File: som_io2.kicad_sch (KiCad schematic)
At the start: 8 parts, among them J1 Hermaphroditic_Molex_203456-0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, Y1 Oscillator_156.25MHz_SG3225EEN

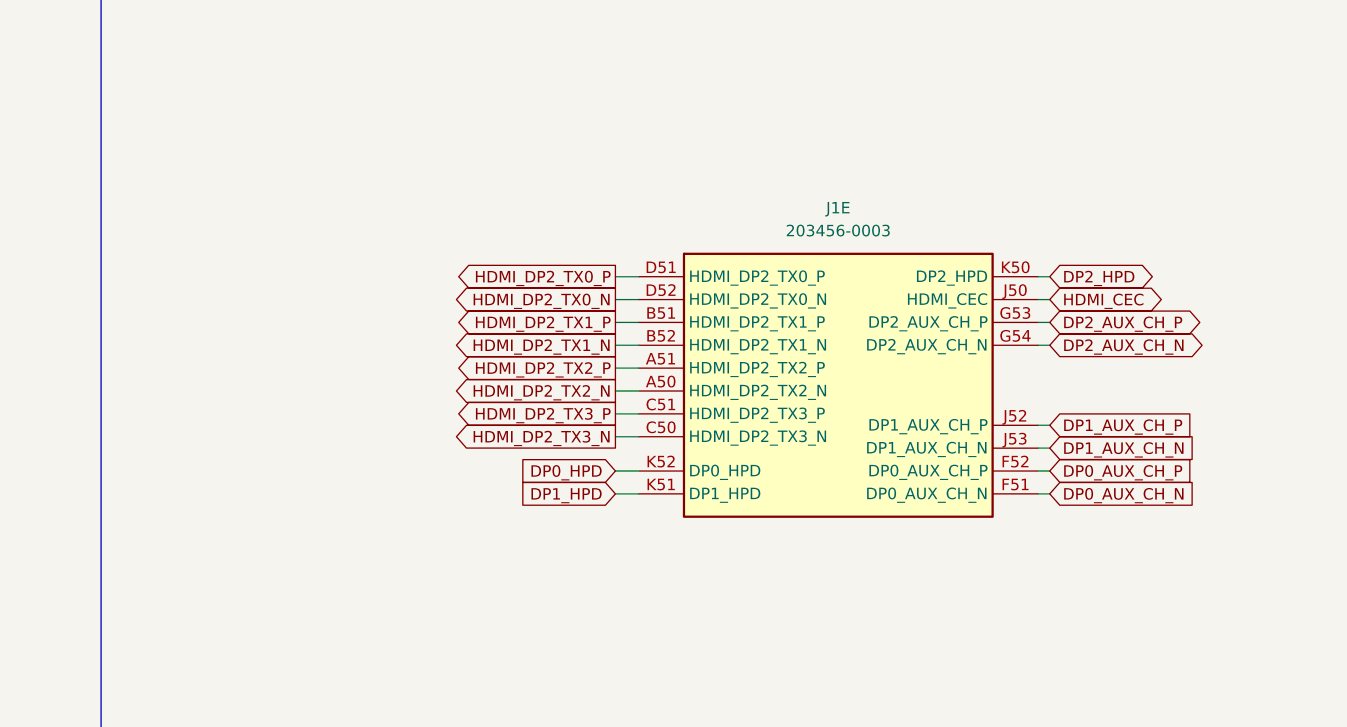
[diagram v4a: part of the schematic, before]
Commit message: [#82837] Start fixing USB DP Alt mode sheet: clean up, define DP bus, rename USB nets and buses to match rest of the schematic
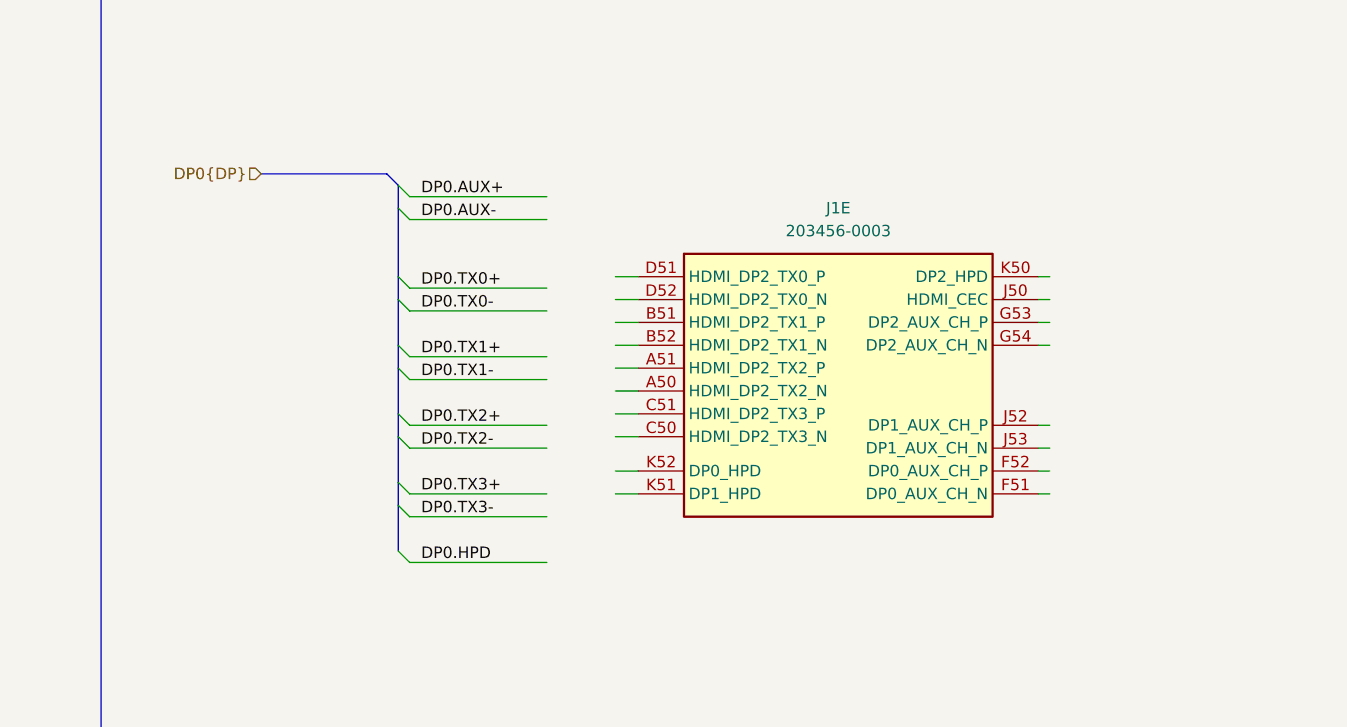
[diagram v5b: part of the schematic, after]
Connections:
- net DP0_AUX_CH_N: no longer names the net of J1.F51 (DP0_AUX_CH_N)
- net DP0_AUX_CH_P: no longer names the net of J1.F52 (DP0_AUX_CH_P)
- net DP0_HPD: no longer names the net of J1.K52 (DP0_HPD)
- net DP1_AUX_CH_N: no longer names the net of J1.J53 (DP1_AUX_CH_N)
- net DP1_AUX_CH_P: no longer names the net of J1.J52 (DP1_AUX_CH_P)
- net DP1_HPD: no longer names the net of J1.K51 (DP1_HPD)
- net DP2_AUX_CH_N: no longer names the net of J1.G54 (DP2_AUX_CH_N)
- net DP2_AUX_CH_P: no longer names the net of J1.G53 (DP2_AUX_CH_P)
- net DP2_HPD: no longer names the net of J1.K50 (DP2_HPD)
- net HDMI_CEC: no longer names the net of J1.J50 (HDMI_CEC)
- net HDMI_DP2_TX0_N: no longer names the net of J1.D52 (HDMI_DP2_TX0_N)
- net HDMI_DP2_TX0_P: no longer names the net of J1.D51 (HDMI_DP2_TX0_P)
- net HDMI_DP2_TX1_N: no longer names the net of J1.B52 (HDMI_DP2_TX1_N)
- net HDMI_DP2_TX1_P: no longer names the net of J1.B51 (HDMI_DP2_TX1_P)
- net HDMI_DP2_TX2_N: no longer names the net of J1.A50 (HDMI_DP2_TX2_N)
- net HDMI_DP2_TX2_P: no longer names the net of J1.A51 (HDMI_DP2_TX2_P)
- net HDMI_DP2_TX3_N: no longer names the net of J1.C50 (HDMI_DP2_TX3_N)
- net HDMI_DP2_TX3_P: no longer names the net of J1.C51 (HDMI_DP2_TX3_P)

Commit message: [#82837] Map interfaces from AGX to Thor on SoM schematic and add level shifters for 1V8 interfaces
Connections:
- net PCIe_{C5x8}.CLK+ is gone; now on net PCIe_{C3x2}.CLK+: J1.F24 (PEX_CLK5_P)
- net PCIe_{C5x8}.CLK- is gone; now on net PCIe_{C3x2}.CLK-: J1.F25 (PEX_CLK5_N)
- net PCIe_{C5x8}.RX0+ is gone; now on net PCIe_{C3x2}.RX0+: J1.D24 (UPHY_RX12_P)
- net PCIe_{C5x8}.RX0- is gone; now on net PCIe_{C3x2}.RX0-: J1.D25 (UPHY_RX12_N)
- net PCIe_{C5x8}.RX1+ is gone; now on net PCIe_{C3x2}.RX1+: J1.B25 (UPHY_RX13_P)
- net PCIe_{C5x8}.RX1- is gone; now on net PCIe_{C3x2}.RX1-: J1.B24 (UPHY_RX13_N)
- net PCIe_{C5x8}.TX0+ is gone; now on net PCIe_{C3x2}.TX0+: J1.H24 (UPHY_TX12_P)
- net PCIe_{C5x8}.TX0- is gone; now on net PCIe_{C3x2}.TX0-: J1.H25 (UPHY_TX12_N)
- net PCIe_{C5x8}.TX1+ is gone; now on net PCIe_{C3x2}.TX1+: J1.K25 (UPHY_TX13_P)
- net PCIe_{C5x8}.TX1- is gone; now on net PCIe_{C3x2}.TX1-: J1.K24 (UPHY_TX13_N)
- net PCIe_{C5x8}.~{CLKREQ} is gone; now on net PCIe_{C3x2}.~{CLKREQ}: J1.C8 (PEX_C5_CLKREQ_N)
- net PCIe_{C5x8}.~{RST} is gone; now on net PCIe_{C3x2}.~{RST}: J1.H10 (PEX_C5_RST_N)
- net PCIe_{C0x1}.CK+ renamed PCIe_{C2x1}.CK+
- net PCIe_{C0x1}.CK- renamed PCIe_{C2x1}.CK-
- net PCIe_{C0x1}.RX0+: no longer names the net of J1.A22 (UPHY_RX0_P)
- net PCIe_{C0x1}.RX0-: no longer names the net of J1.A23 (UPHY_RX0_N)
- net PCIe_{C0x1}.TX0+: no longer names the net of J1.J22 (UPHY_TX0_P)
- net PCIe_{C0x1}.TX0-: no longer names the net of J1.J23 (UPHY_TX0_N)
- net PCIe_{C0x1}.~{CLKREQ} renamed PCIe_{C2x1}.~{CLKREQ}
- net PCIe_{C4x4}.CLK+ renamed PCIe_{C3x2}.CLK+
- net PCIe_{C4x4}.CLK- renamed PCIe_{C3x2}.CLK-
- net PCIe_{C4x4}.RX0+: no longer names the net of J1.D33 (UPHY_RX22_P)
- net PCIe_{C4x4}.RX0-: no longer names the net of J1.D32 (UPHY_RX22_N)
- net PCIe_{C4x4}.RX1+ renamed PCIe_{C2x1}.RX0+
- net PCIe_{C4x4}.RX1- renamed PCIe_{C2x1}.RX0-
- net PCIe_{C4x4}.RX2+ renamed PCIe_{C3x2}.RX0+
- net PCIe_{C4x4}.RX2- renamed PCIe_{C3x2}.RX0-
- net PCIe_{C4x4}.RX3+ renamed PCIe_{C3x2}.RX1+
- net PCIe_{C4x4}.RX3- renamed PCIe_{C3x2}.RX1-
- net PCIe_{C4x4}.TX0+: no longer names the net of J1.J35 (UPHY_TX22_P)
- net PCIe_{C4x4}.TX0-: no longer names the net of J1.J34 (UPHY_TX22_N)
- net PCIe_{C4x4}.TX1+ renamed PCIe_{C2x1}.TX0+
- net PCIe_{C4x4}.TX1- renamed PCIe_{C2x1}.TX0-
- net PCIe_{C4x4}.TX2+ renamed PCIe_{C3x2}.TX0+
- net PCIe_{C4x4}.TX2- renamed PCIe_{C3x2}.TX0-
- net PCIe_{C4x4}.TX3+ renamed PCIe_{C3x2}.TX1+
- net PCIe_{C4x4}.TX3- renamed PCIe_{C3x2}.TX1-
- net PCIe_{C4x4}.~{CLKREQ} renamed PCIe_{C3x2}.~{CLKREQ}
- net PCIe_{C4x4}.~{RST} renamed PCIe_{C3x2}.~{RST}
- net PCIe_{C5x8}.RX2+ renamed PCIe_{C3x2}.RX2+
- net PCIe_{C5x8}.RX2- renamed PCIe_{C3x2}.RX2-
- net PCIe_{C5x8}.RX3+ renamed PCIe_{C3x2}.RX3+
- net PCIe_{C5x8}.RX3- renamed PCIe_{C3x2}.RX3-
- net PCIe_{C5x8}.RX4+: no longer names the net of J1.D28 (UPHY_RX16_P)
- net PCIe_{C5x8}.RX4-: no longer names the net of J1.D29 (UPHY_RX16_N)
- net PCIe_{C5x8}.RX5+: no longer names the net of J1.B29 (UPHY_RX17_P)
- net PCIe_{C5x8}.RX5-: no longer names the net of J1.B28 (UPHY_RX17_N)
- net PCIe_{C5x8}.RX6+: no longer names the net of J1.C31 (UPHY_RX18_P)
- net PCIe_{C5x8}.RX6-: no longer names the net of J1.C30 (UPHY_RX18_N)
- net PCIe_{C5x8}.RX7+: no longer names the net of J1.A30 (UPHY_RX19_P)
- net PCIe_{C5x8}.RX7-: no longer names the net of J1.A31 (UPHY_RX19_N)
- net PCIe_{C5x8}.TX2+ renamed PCIe_{C3x2}.TX2+
- net PCIe_{C5x8}.TX2- renamed PCIe_{C3x2}.TX2-
- net PCIe_{C5x8}.TX3+ renamed PCIe_{C3x2}.TX3+
- net PCIe_{C5x8}.TX3- renamed PCIe_{C3x2}.TX3-
- net PCIe_{C5x8}.TX4+: no longer names the net of J1.H28 (UPHY_TX16_P)
- net PCIe_{C5x8}.TX4-: no longer names the net of J1.H29 (UPHY_TX16_N)
- net PCIe_{C5x8}.TX5+: no longer names the net of J1.K29 (UPHY_TX17_P)
- net PCIe_{C5x8}.TX5-: no longer names the net of J1.K28 (UPHY_TX17_N)
- net PCIe_{C5x8}.TX6+: no longer names the net of J1.G31 (UPHY_TX18_P)
- net PCIe_{C5x8}.TX6-: no longer names the net of J1.G30 (UPHY_TX18_N)
- net PCIe_{C5x8}.TX7+: no longer names the net of J1.J30 (UPHY_TX19_P)
- net PCIe_{C5x8}.TX7-: no longer names the net of J1.J31 (UPHY_TX19_N)
- net RGMII.MDC: no longer names the net of J1.E6 (RGMII_SMA_MDC)
- net RGMII.MDIO: no longer names the net of J1.E7 (RGMII_SMA_MDIO)
- net RGMII.RD0: no longer names the net of J1.C4 (RGMII_RD0)
- net RGMII.RD1: no longer names the net of J1.K6 (RGMII_RD1)
- net RGMII.RD2: no longer names the net of J1.H6 (RGMII_RD2)
- net RGMII.RD3: no longer names the net of J1.E5 (RGMII_RD3)
- net RGMII.RXC: no longer names the net of J1.C5 (RGMII_RXC)
- net RGMII.RX_CTL: no longer names the net of J1.D5 (RGMII_RX_CTL)
- net RGMII.TD0: no longer names the net of J1.J6 (RGMII_TD0)
- net RGMII.TD1: no longer names the net of J1.G5 (RGMII_TD1)
- net RGMII.TD2: no longer names the net of J1.J7 (RGMII_TD2)
- net RGMII.TD3: no longer names the net of J1.G6 (RGMII_TD3)
- net RGMII.TXC: no longer names the net of J1.B5 (RGMII_TXC)
- net RGMII.TX_CTL: no longer names the net of J1.K7 (RGMII_TX_CTL)
- net RGMII.~{INT}: no longer names the net of J1.J5 (ENET_INT)
- net RGMII.~{RST}: no longer names the net of J1.H5 (ENET_RST_N)
- net UPHY_REFCLK0_N: no longer names the net of J1.E31 (UPHY_REFCLK0_N)
- net UPHY_REFCLK0_P: no longer names the net of J1.E30 (UPHY_REFCLK0_P)
- net UPHY_REFCLK1_N: no longer names the net of J1.E26 (UPHY_REFCLK1_N)
- net UPHY_REFCLK1_P: no longer names the net of J1.E27 (UPHY_REFCLK1_P)
- net UPHY_REFCLK3_N: no longer names the net of J1.F33 (UPHY_REFCLK3_N)
- net UPHY_REFCLK3_P: no longer names the net of J1.F32 (UPHY_REFCLK3_P)
- net UPHY_REFCLK4_N: no longer names the net of J1.C38 (UPHY_REFCLK4_N)
- net UPHY_REFCLK4_P: no longer names the net of J1.C39 (UPHY_REFCLK4_P)

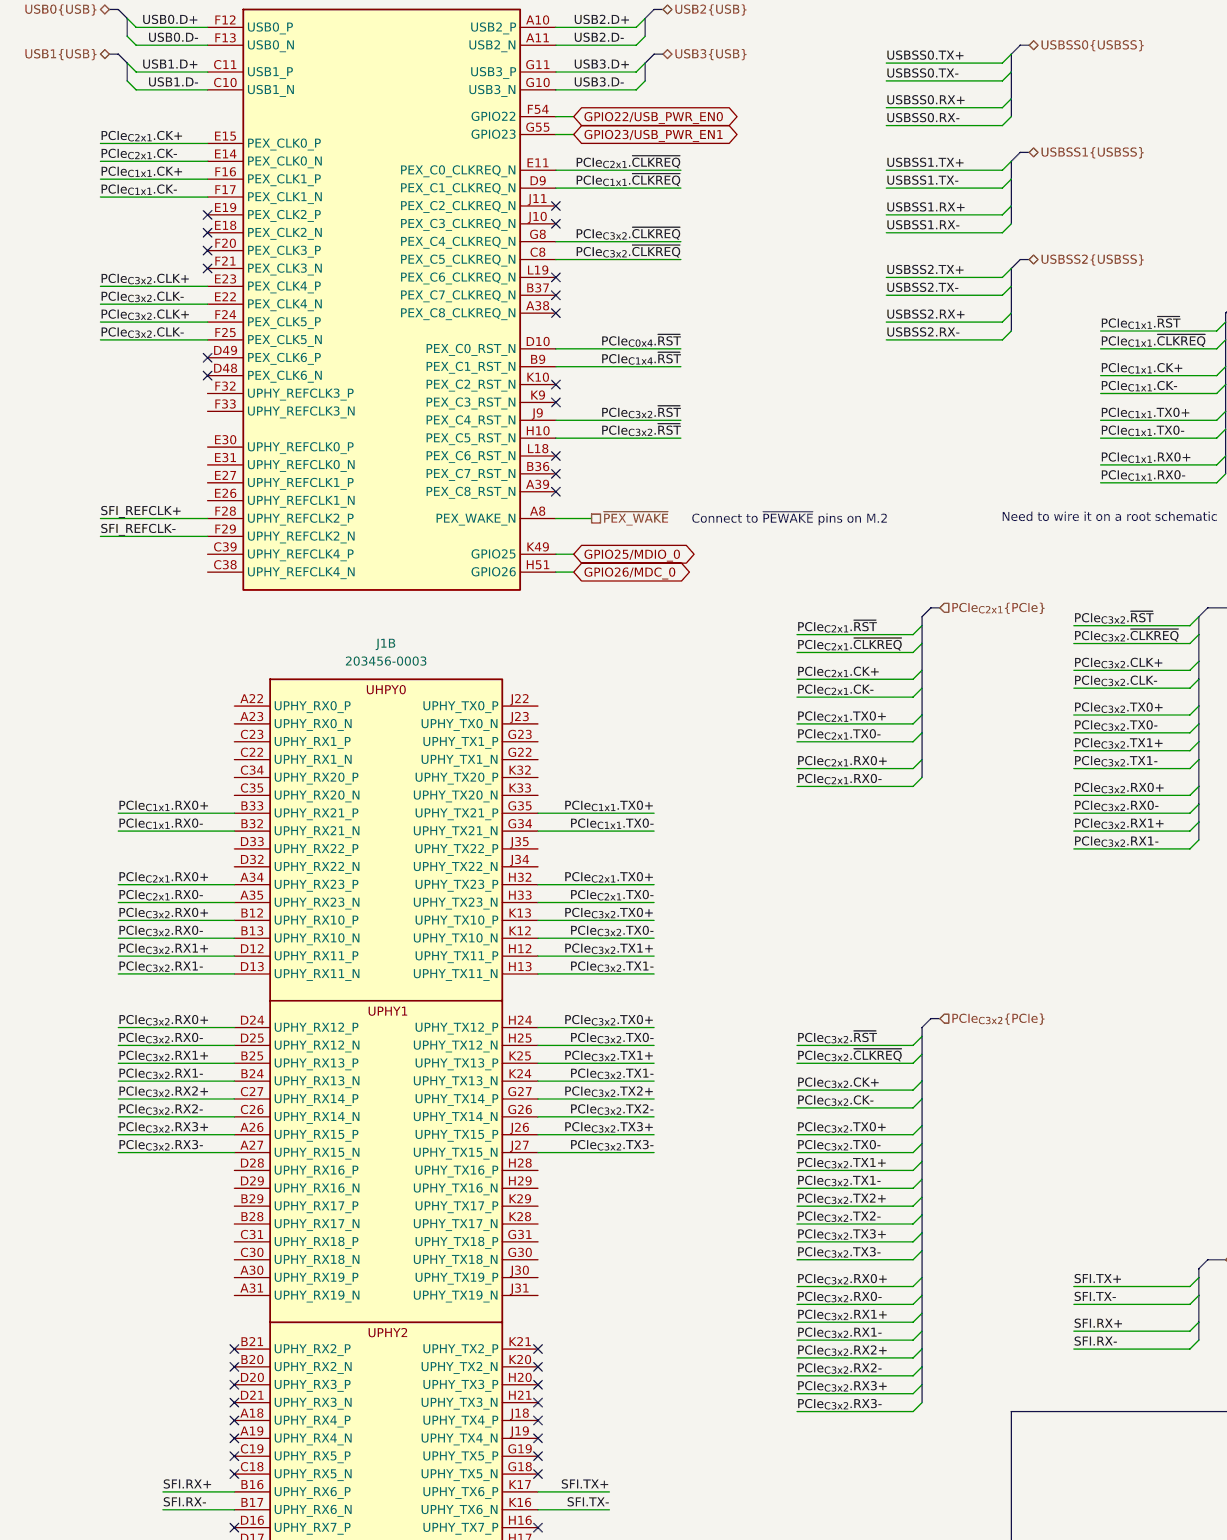
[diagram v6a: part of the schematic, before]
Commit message: [#82837] Finish mapping interfaces, waiting for new SoM symbol
[#82837] Add GPIO level shifter and route USB related GPIO on root
schematic

[#82837] WIP: Modify Power-up and reset section
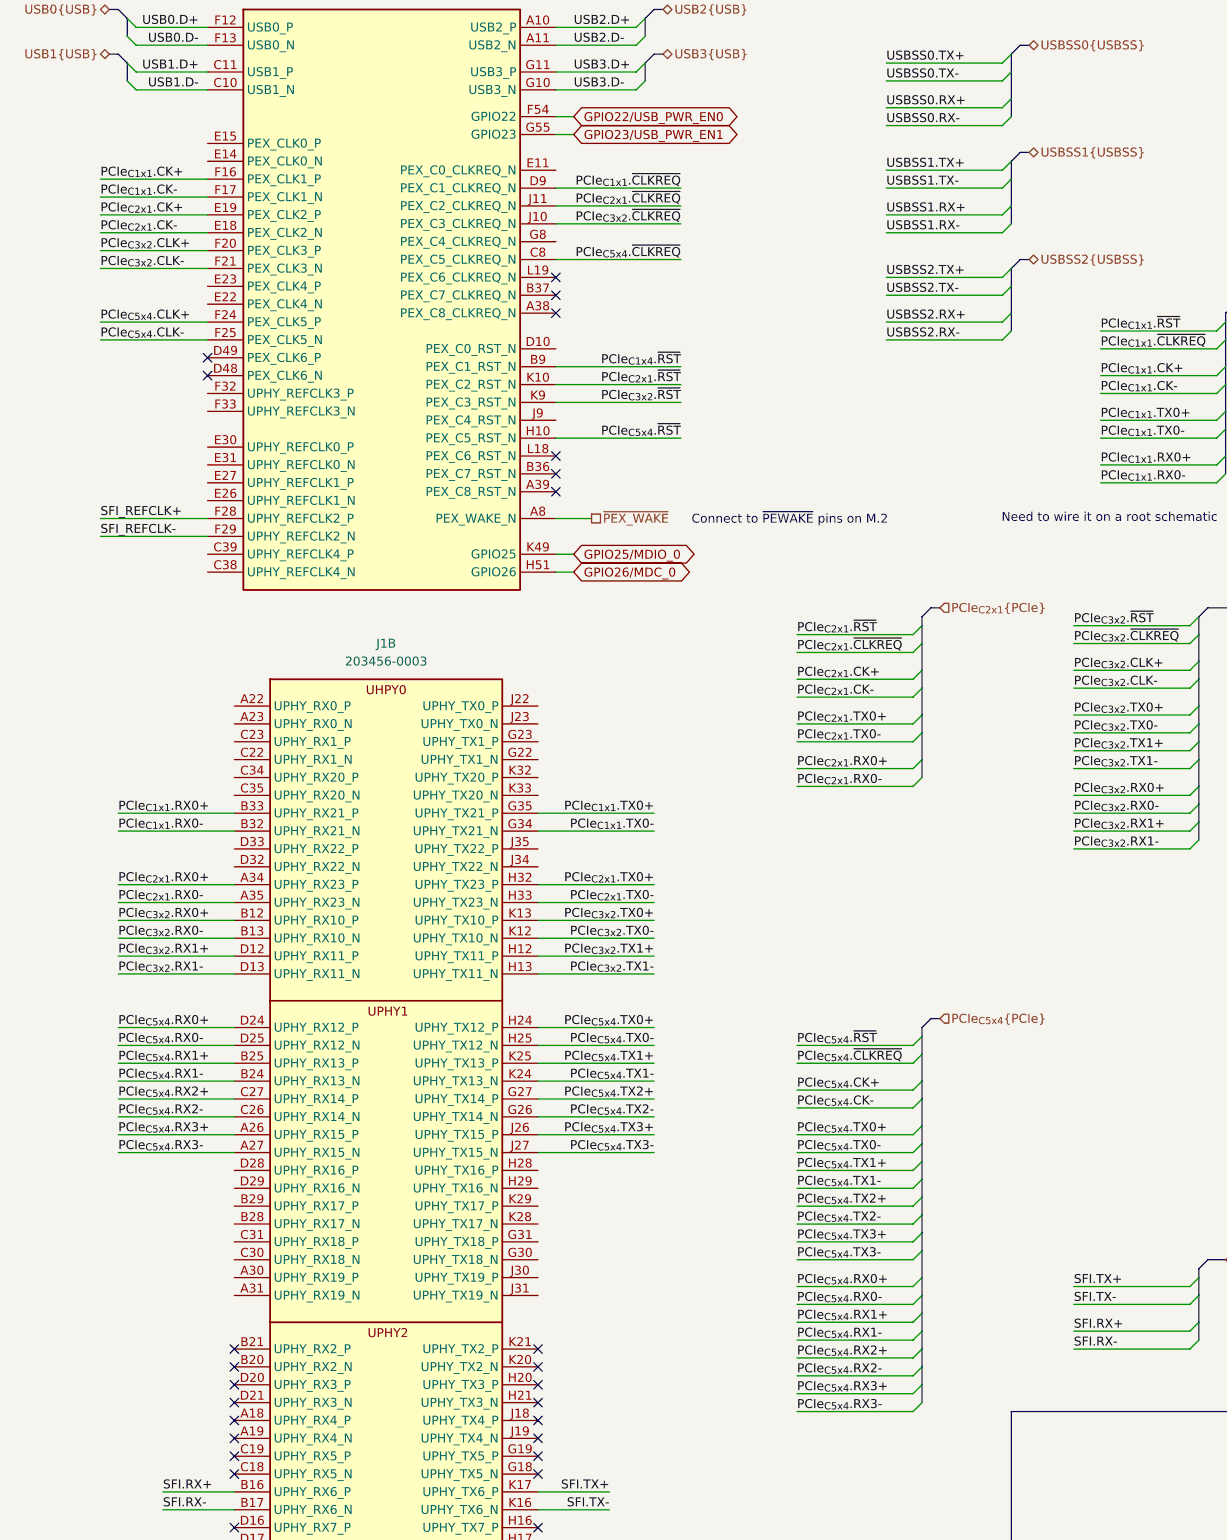
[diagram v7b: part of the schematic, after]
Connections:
- net PCIe_{C2x1}.CK+: now also J1.E19 (PEX_CLK2_P); no longer J1.E15 (PEX_CLK0_P)
- net PCIe_{C2x1}.CK-: now also J1.E18 (PEX_CLK2_N); no longer J1.E14 (PEX_CLK0_N)
- net PCIe_{C2x1}.~{CLKREQ}: now also J1.J11 (PEX_C2_CLKREQ_N); no longer J1.E11 (PEX_C0_CLKREQ_N)
- net PCIe_{C2x1}.~{RST}: now also J1.K10 (PEX_C2_RST_N)
- net PCIe_{C3x2}.CLK+: now also J1.F20 (PEX_CLK3_P); no longer J1.E23 (PEX_CLK4_P), J1.F24 (PEX_CLK5_P)
- net PCIe_{C3x2}.CLK-: now also J1.F21 (PEX_CLK3_N); no longer J1.E22 (PEX_CLK4_N), J1.F25 (PEX_CLK5_N)
- net PCIe_{C3x2}.RX0+: no longer J1.D24 (UPHY_RX12_P)
- net PCIe_{C3x2}.RX0-: no longer J1.D25 (UPHY_RX12_N)
- net PCIe_{C3x2}.RX1+: no longer J1.B25 (UPHY_RX13_P)
- net PCIe_{C3x2}.RX1-: no longer J1.B24 (UPHY_RX13_N)
- net PCIe_{C3x2}.TX0+: no longer J1.H24 (UPHY_TX12_P)
- net PCIe_{C3x2}.TX0-: no longer J1.H25 (UPHY_TX12_N)
- net PCIe_{C3x2}.TX1+: no longer J1.K25 (UPHY_TX13_P)
- net PCIe_{C3x2}.TX1-: no longer J1.K24 (UPHY_TX13_N)
- net PCIe_{C3x2}.~{CLKREQ}: now also J1.J10 (PEX_C3_CLKREQ_N); no longer J1.C8 (PEX_C5_CLKREQ_N), J1.G8 (PEX_C4_CLKREQ_N)
- net PCIe_{C3x2}.~{RST}: now also J1.K9 (PEX_C3_RST_N); no longer J1.H10 (PEX_C5_RST_N), J1.J9 (PEX_C4_RST_N)
- net PCIe_{C0x4}.~{RST}: no longer names the net of J1.D10 (PEX_C0_RST_N)
- net PCIe_{C3x2}.RX2+ renamed PCIe_{C5x4}.RX2+
- net PCIe_{C3x2}.RX2- renamed PCIe_{C5x4}.RX2-
- net PCIe_{C3x2}.RX3+ renamed PCIe_{C5x4}.RX3+
- net PCIe_{C3x2}.RX3- renamed PCIe_{C5x4}.RX3-
- net PCIe_{C3x2}.TX2+ renamed PCIe_{C5x4}.TX2+
- net PCIe_{C3x2}.TX2- renamed PCIe_{C5x4}.TX2-
- net PCIe_{C3x2}.TX3+ renamed PCIe_{C5x4}.TX3+
- net PCIe_{C3x2}.TX3- renamed PCIe_{C5x4}.TX3-
- new net PCIe_{C5x4}.CLK+: J1.F24 (PEX_CLK5_P)
- new net PCIe_{C5x4}.CLK-: J1.F25 (PEX_CLK5_N)
- new net PCIe_{C5x4}.RX0+: J1.D24 (UPHY_RX12_P)
- new net PCIe_{C5x4}.RX0-: J1.D25 (UPHY_RX12_N)
- new net PCIe_{C5x4}.RX1+: J1.B25 (UPHY_RX13_P)
- new net PCIe_{C5x4}.RX1-: J1.B24 (UPHY_RX13_N)
- new net PCIe_{C5x4}.TX0+: J1.H24 (UPHY_TX12_P)
- new net PCIe_{C5x4}.TX0-: J1.H25 (UPHY_TX12_N)
- new net PCIe_{C5x4}.TX1+: J1.K25 (UPHY_TX13_P)
- new net PCIe_{C5x4}.TX1-: J1.K24 (UPHY_TX13_N)
- new net PCIe_{C5x4}.~{CLKREQ}: J1.C8 (PEX_C5_CLKREQ_N)
- new net PCIe_{C5x4}.~{RST}: J1.H10 (PEX_C5_RST_N)
- no-connect marks 52 -> 44
